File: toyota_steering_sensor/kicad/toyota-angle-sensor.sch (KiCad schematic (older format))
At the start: 32 parts, among them IC1 ATMEGA328PB-AU, IC2 LS7366R, IC3 AS5047P, J1 AVR-ISP-6, J2 RJ45, U1 NCP1117-5.0_SOT223, U2 MCP2515-xSO, U3 TJA1051T-3, Y1 16MHz, Y2 40MHz, Y3 8MHz

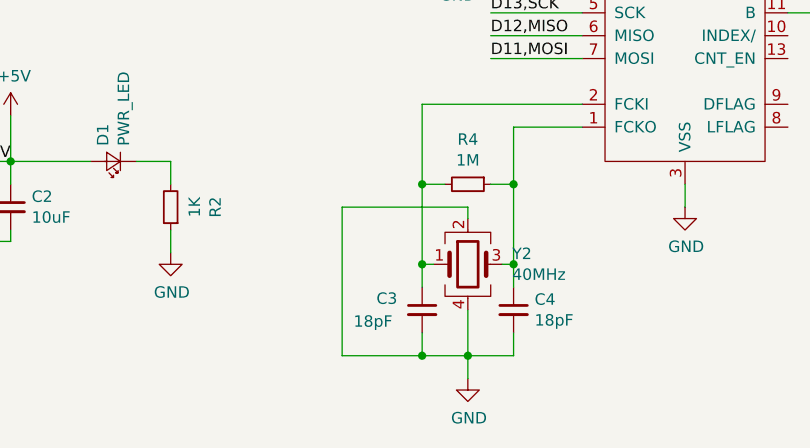
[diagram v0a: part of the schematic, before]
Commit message: change resistor and capacitor from 0402 to 0603
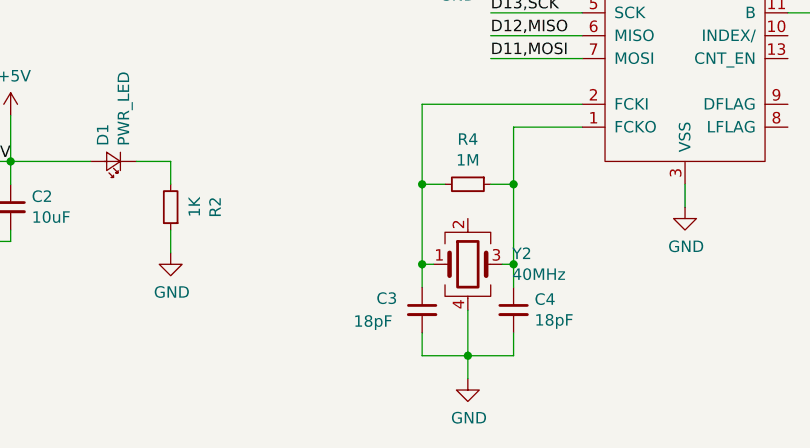
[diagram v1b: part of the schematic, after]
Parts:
- C10, C11, C12, C3, C4, C5, C6, C7, C8, C9: footprint Capacitor_SMD:C_0402_1005Metric -> Capacitor_SMD:C_0603_1608Metric
- R1, R2, R3, R4, R5, R6, R7: footprint Resistor_SMD:R_0402_1005Metric -> Resistor_SMD:R_0603_1608Metric
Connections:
- net GND: no longer Y2.2
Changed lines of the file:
@@
 F 0 "R1" H 1559 1146 50  0000 L CNN
 F 1 "10K" H 1559 1055 50  0000 L CNN
-F 2 "Resistor_SMD:R_0402_1005Metric" H 1500 1100 50  0001 C CNN
+F 2 "Resistor_SMD:R_0603_1608Metric" H 1500 1100 50  0001 C CNN
 F 3 "~" H 1500 1100 50  0001 C CNN
 	1    1500 1100
@@
 F 0 "C5" V 4321 2250 50  0000 C CNN
 F 1 "27pF" V 4412 2250 50  0000 C CNN
-F 2 "Capacitor_SMD:C_0402_1005Metric" H 4550 2250 50  0001 C CNN
+F 2 "Capacitor_SMD:C_0603_1608Metric" H 4550 2250 50  0001 C CNN
 F 3 "~" H 4550 2250 50  0001 C CNN
 	1    4550 2250
@@
 F 0 "C6" V 4413 2550 50  0000 C CNN
 F 1 "27pF" V 4412 2550 50  0001 C CNN
-F 2 "Capacitor_SMD:C_0402_1005Metric" H 4550 2550 50  0001 C CNN
+F 2 "Capacitor_SMD:C_0603_1608Metric" H 4550 2550 50  0001 C CNN
 F 3 "~" H 4550 2550 50  0001 C CNN
 	1    4550 2550
@@
 F 0 "R5" H 6459 2646 50  0000 L CNN
 F 1 "10K" H 6459 2555 50  0000 L CNN
-F 2 "Resistor_SMD:R_0402_1005Metric" H 6400 2600 50  0001 C CNN
+F 2 "Resistor_SMD:R_0603_1608Metric" H 6400 2600 50  0001 C CNN
 F 3 "~" H 6400 2600 50  0001 C CNN
 	1    6400 2600
@@
 F 0 "C7" V 8050 4100 50  0000 C CNN
 F 1 "1uF" V 7950 4100 50  0000 C CNN
-F 2 "Capacitor_SMD:C_0402_1005Metric" H 7850 4100 50  0001 C CNN
+F 2 "Capacitor_SMD:C_0603_1608Metric" H 7850 4100 50  0001 C CNN
 F 3 "~" H 7850 4100 50  0001 C CNN
 	1    7850 4100
@@
 F 0 "R3" H 3659 2696 50  0000 L CNN
 F 1 "1K" H 3659 2605 50  0000 L CNN
-F 2 "Resistor_SMD:R_0402_1005Metric" H 3600 2650 50  0001 C CNN
+F 2 "Resistor_SMD:R_0603_1608Metric" H 3600 2650 50  0001 C CNN
 F 3 "~" H 3600 2650 50  0001 C CNN
 	1    3600 2650
@@
 F 0 "C4" H 4342 5846 50  0000 L CNN
 F 1 "18pF" H 4342 5755 50  0000 L CNN
-F 2 "Capacitor_SMD:C_0402_1005Metric" H 4250 5800 50  0001 C CNN
+F 2 "Capacitor_SMD:C_0603_1608Metric" H 4250 5800 50  0001 C CNN
 F 3 "~" H 4250 5800 50  0001 C CNN
 	1    4250 5800
@@
 F 0 "R4" V 3854 5250 50  0000 C CNN
 F 1 "1M" V 3945 5250 50  0000 C CNN
-F 2 "Resistor_SMD:R_0402_1005Metric" H 4050 5250 50  0001 C CNN
+F 2 "Resistor_SMD:R_0603_1608Metric" H 4050 5250 50  0001 C CNN
 F 3 "~" H 4050 5250 50  0001 C CNN
 	1    4050 5250
@@
 F 0 "C3" H 3650 5850 50  0000 L CNN
 F 1 "18pF" H 3550 5750 50  0000 L CNN
-F 2 "Capacitor_SMD:C_0402_1005Metric" H 3850 5800 50  0001 C CNN
+F 2 "Capacitor_SMD:C_0603_1608Metric" H 3850 5800 50  0001 C CNN
 F 3 "~" H 3850 5800 50  0001 C CNN
 	1    3850 5800
@@
 F 0 "R7" H 6659 4746 50  0000 L CNN
 F 1 "10K" H 6659 4655 50  0000 L CNN
-F 2 "Resistor_SMD:R_0402_1005Metric" H 6600 4700 50  0001 C CNN
+F 2 "Resistor_SMD:R_0603_1608Metric" H 6600 4700 50  0001 C CNN
 F 3 "~" H 6600 4700 50  0001 C CNN
 	1    6600 4700
@@
 F 0 "C12" H 8392 3696 50  0000 L CNN
 F 1 ".1uF" H 8392 3605 50  0000 L CNN
-F 2 "Capacitor_SMD:C_0402_1005Metric" H 8300 3650 50  0001 C CNN
+F 2 "Capacitor_SMD:C_0603_1608Metric" H 8300 3650 50  0001 C CNN
 F 3 "~" H 8300 3650 50  0001 C CNN
 	1    8300 3650
@@
 F 0 "C9" H 4092 4196 50  0000 L CNN
 F 1 ".1uF" H 4092 4105 50  0000 L CNN
-F 2 "Capacitor_SMD:C_0402_1005Metric" H 4000 4150 50  0001 C CNN
+F 2 "Capacitor_SMD:C_0603_1608Metric" H 4000 4150 50  0001 C CNN
 F 3 "~" H 4000 4150 50  0001 C CNN
 	1    4000 4150
@@
 F 0 "C8" H 1242 3296 50  0000 L CNN
 F 1 ".1uF" H 1242 3205 50  0000 L CNN
-F 2 "Capacitor_SMD:C_0402_1005Metric" H 1150 3250 50  0001 C CNN
+F 2 "Capacitor_SMD:C_0603_1608Metric" H 1150 3250 50  0001 C CNN
 F 3 "~" H 1150 3250 50  0001 C CNN
 	1    1150 3250
@@
 F 0 "C10" H 4642 1396 50  0000 L CNN
 F 1 ".1uF" H 4642 1305 50  0000 L CNN
-F 2 "Capacitor_SMD:C_0402_1005Metric" H 4550 1350 50  0001 C CNN
+F 2 "Capacitor_SMD:C_0603_1608Metric" H 4550 1350 50  0001 C CNN
 F 3 "~" H 4550 1350 50  0001 C CNN
 	1    4550 1350
@@
 F 0 "C11" H 8192 1246 50  0000 L CNN
 F 1 ".1uF" H 8192 1155 50  0000 L CNN
-F 2 "Capacitor_SMD:C_0402_1005Metric" H 8100 1200 50  0001 C CNN
+F 2 "Capacitor_SMD:C_0603_1608Metric" H 8100 1200 50  0001 C CNN
 F 3 "~" H 8100 1200 50  0001 C CNN
 	1    8100 1200
@@
 F 0 "R2" V 2554 5350 50  0000 C CNN
 F 1 "1K" V 2645 5350 50  0000 C CNN
-F 2 "Resistor_SMD:R_0402_1005Metric" H 2750 5350 50  0001 C CNN
+F 2 "Resistor_SMD:R_0603_1608Metric" H 2750 5350 50  0001 C CNN
 F 3 "~" H 2750 5350 50  0001 C CNN
 	1    2750 5350
@@
 F 0 "R6" H 6459 3746 50  0000 L CNN
 F 1 "10K" H 6459 3655 50  0000 L CNN
-F 2 "Resistor_SMD:R_0402_1005Metric" H 6400 3700 50  0001 C CNN
+F 2 "Resistor_SMD:R_0603_1608Metric" H 6400 3700 50  0001 C CNN
 F 3 "~" H 6400 3700 50  0001 C CNN
 	1    6400 3700
 	1    0    0    -1
 $EndComp
-Wire Wire Line
-	4050 5400 4050 5350
-Wire Wire Line
-	4050 5350 3500 5350
-Wire Wire Line
-	3500 5350 3500 6000
-Wire Wire Line
-	3500 6000 3850 6000
-Connection ~ 3850 6000
 $EndSCHEMATC

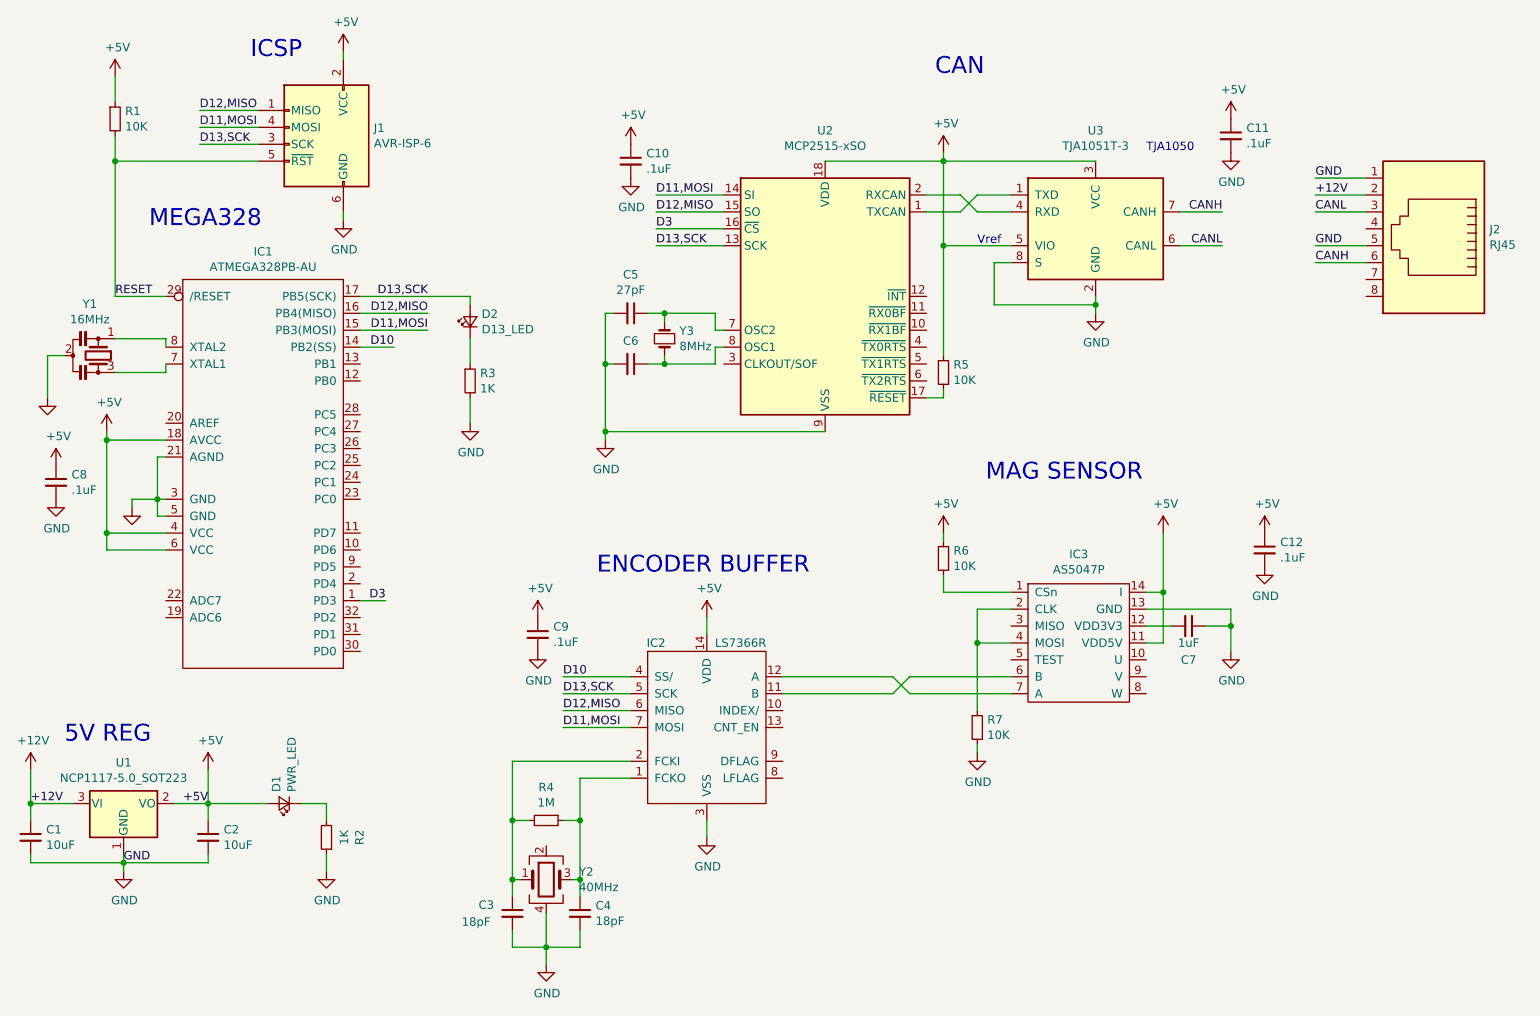
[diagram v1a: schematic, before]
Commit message: modified component ref for BOM
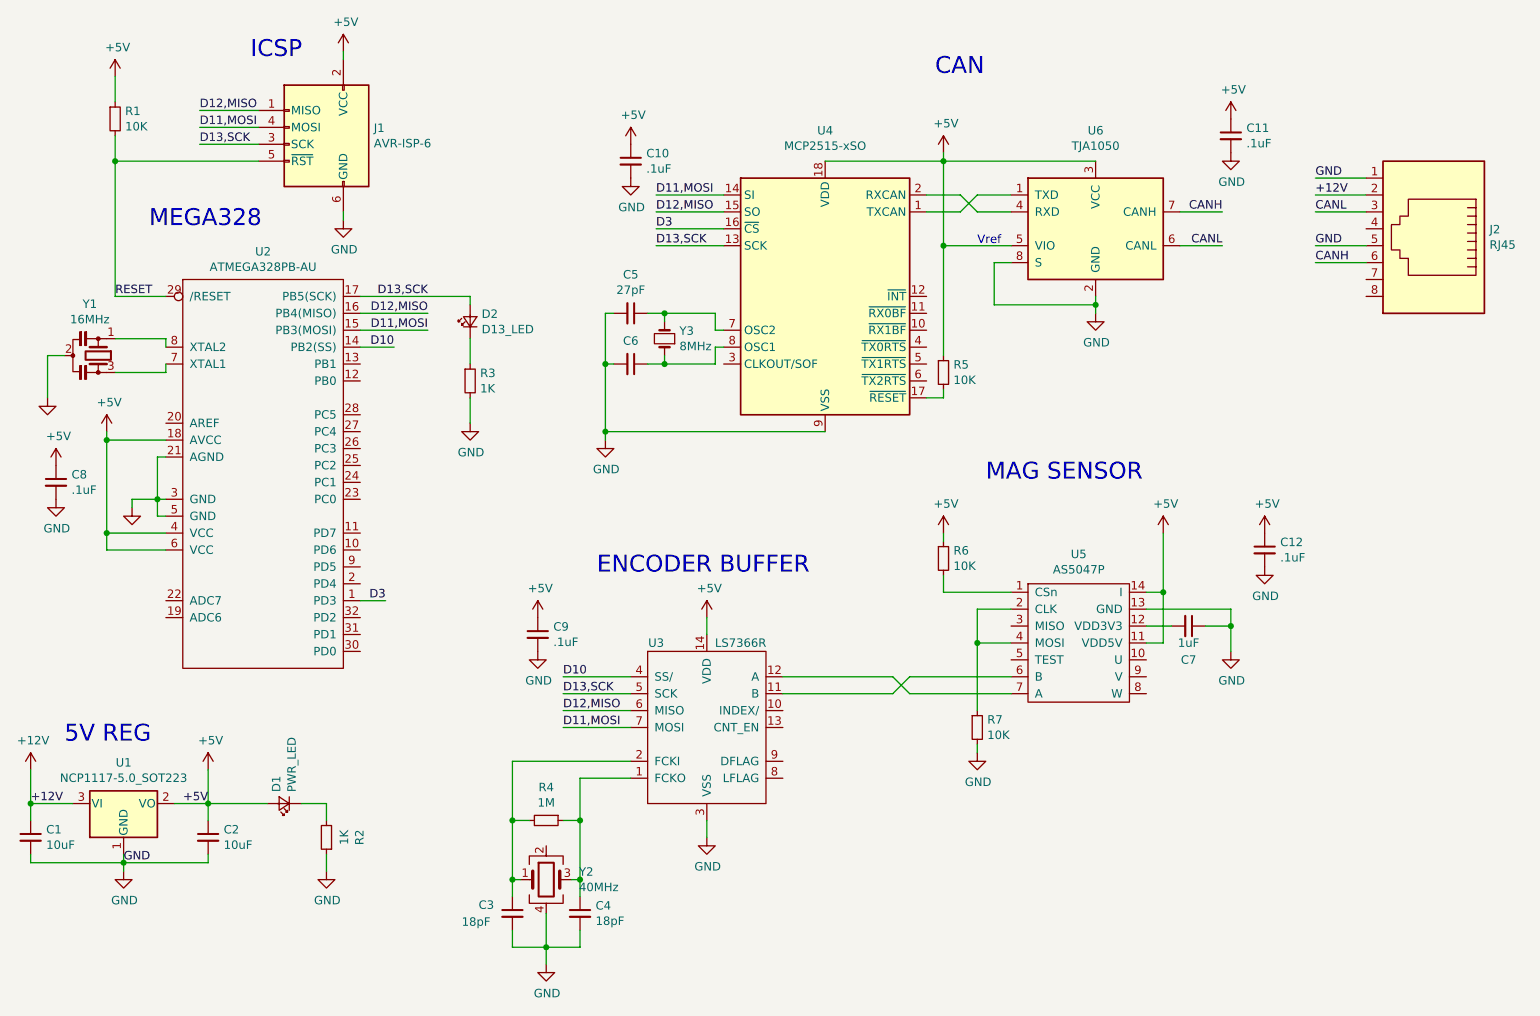
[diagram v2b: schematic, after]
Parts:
- C1, C2: Digi-Key Part Number (none) -> 490-14536-1-ND
- C10, C11, C12, C8, C9: Digi-Key Part Number (none) -> 1276-1000-1-ND
- C3, C4: Digi-Key Part Number (none) -> 1276-2208-1-ND
- C5, C6: Digi-Key Part Number (none) -> 1276-1086-1-ND
- C7: Digi-Key Part Number (none) -> 490-12297-1-ND
- D1, D2: Digi-Key Part Number (none) -> 475-1410-1-ND
- J1: Digi-Key Part Number (none) -> N/A
- J2: Digi-Key Part Number (none) -> 609-1046-ND
- R1, R5, R6, R7: Digi-Key Part Number (none) -> A130097CT-ND
- R2, R3: Digi-Key Part Number (none) -> A130091CT-ND
- R4: Digi-Key Part Number (none) -> A130109CT-ND
- U1: Digi-Key Part Number (none) -> NCP1117ST50T3GOSCT-ND
- U2: renamed from IC1; Digi-Key Part Number (none) -> ATMEGA328PB-AU-ND
- U3: renamed from IC2; Digi-Key Part Number (none) -> N/A
- U4: renamed from U2; Digi-Key Part Number (none) -> MCP2515T-I/SOCT-ND
- U5: renamed from IC3; Digi-Key Part Number (none) -> AS5047P-ATSMCT-ND
- U6: renamed from U3; value TJA1051T-3 -> TJA1050; Digi-Key Part Number (none) -> 568-10292-1-ND
- Y1: Digi-Key Part Number (none) -> 490-17948-1-ND
- Y2: Digi-Key Part Number (none) -> 535-13401-1-ND
- Y3: Digi-Key Part Number (none) -> 535-10630-1-ND
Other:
- note removed: "TJA1050"
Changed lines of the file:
@@
 F 2 "Connector_PinHeader_2.54mm:PinHeader_2x03_P2.54mm_Vertical" V 2500 1300 50  0001 C CNN
 F 3 " ~" H 1475 700 50  0001 C CNN
+F 4 "N/A" H 2750 1250 50  0001 C CNN "Digi-Key Part Number"
 	1    2750 1250
 	-1   0    0    -1
@@
 F 2 "Resistor_SMD:R_0603_1608Metric" H 1500 1100 50  0001 C CNN
 F 3 "~" H 1500 1100 50  0001 C CNN
+F 4 "A130097CT-ND" H 1500 1100 50  0001 C CNN "Digi-Key Part Number"
 	1    1500 1100
 	1    0    0    -1
@@
 F 2 "Package_TO_SOT_SMD:SOT-223-3_TabPin2" H 1550 5350 50  0001 C CNN
 F 3 "http://www.onsemi.com/pub_link/Collateral/NCP1117-D.PDF" H 1650 4900 50  0001 C CNN
+F 4 "NCP1117ST50T3GOSCT-ND" H 1550 5150 50  0001 C CNN "Digi-Key Part Number"
 	1    1550 5150
 	1    0    0    -1
@@
 F 2 "Capacitor_SMD:C_1210_3225Metric" H 1000 5350 50  0001 C CNN
 F 3 "~" H 1000 5350 50  0001 C CNN
+F 4 "490-14536-1-ND" H 1000 5350 50  0001 C CNN "Digi-Key Part Number"
 	1    1000 5350
 	1    0    0    -1
@@
 F 2 "Capacitor_SMD:C_1210_3225Metric" H 2050 5350 50  0001 C CNN
 F 3 "~" H 2050 5350 50  0001 C CNN
+F 4 "490-14536-1-ND" H 2050 5350 50  0001 C CNN "Digi-Key Part Number"
 	1    2050 5350
 	1    0    0    -1
@@
 CAN
 $Comp
-L Interface_CAN_LIN:TJA1051T-3 U3
+L Interface_CAN_LIN:TJA1051T-3 U6
 U 1 1 5D47EE70
 P 7300 1750
-F 0 "U3" H 7300 2331 50  0000 C CNN
-F 1 "TJA1051T-3" H 7300 2240 50  0000 C CNN
+F 0 "U6" H 7300 2331 50  0000 C CNN
+F 1 "TJA1050" H 7300 2240 50  0000 C CNN
 F 2 "Package_SO:SOIC-8_3.9x4.9mm_P1.27mm" H 7300 1250 50  0001 C CIN
 F 3 "http://www.nxp.com/documents/data_sheet/TJA1051.pdf" H 7300 1750 50  0001 C CNN
+F 4 "568-10292-1-ND" H 7300 1750 50  0001 C CNN "Digi-Key Part Number"
 	1    7300 1750
 	1    0    0    -1
 $EndComp
-Text Notes 7600 1300 0    50   ~ 0
-TJA1050
 Text Notes 6600 1850 0    50   ~ 0
 Vref
@@
 F 2 "Crystal:Crystal_SMD_Abracon_ABM3-2Pin_5.0x3.2mm_HandSoldering" H 4750 2400 50  0001 C CNN
 F 3 "~" H 4750 2400 50  0001 C CNN
+F 4 "535-10630-1-ND" H 4750 2400 50  0001 C CNN "Digi-Key Part Number"
 	1    4750 2400
 	0    -1   -1   0
@@
 F 2 "Capacitor_SMD:C_0603_1608Metric" H 4550 2250 50  0001 C CNN
 F 3 "~" H 4550 2250 50  0001 C CNN
+F 4 "1276-1086-1-ND " H 4550 2250 50  0001 C CNN "Digi-Key Part Number"
 	1    4550 2250
 	0    1    1    0
@@
 F 2 "Capacitor_SMD:C_0603_1608Metric" H 4550 2550 50  0001 C CNN
 F 3 "~" H 4550 2550 50  0001 C CNN
+F 4 "1276-1086-1-ND " H 4550 2550 50  0001 C CNN "Digi-Key Part Number"
 	1    4550 2550
 	0    1    1    0
@@
 F 2 "Resistor_SMD:R_0603_1608Metric" H 6400 2600 50  0001 C CNN
 F 3 "~" H 6400 2600 50  0001 C CNN
+F 4 "A130097CT-ND" H 6400 2600 50  0001 C CNN "Digi-Key Part Number"
 	1    6400 2600
 	1    0    0    -1
@@
 CANH
 $Comp
-L Angle_Sensor:AS5047P IC3
+L Angle_Sensor:AS5047P U5
 U 1 1 5D4CF604
 P 7200 3800
-F 0 "IC3" H 7200 3925 50  0000 C CNN
+F 0 "U5" H 7200 3925 50  0000 C CNN
 F 1 "AS5047P" H 7200 3834 50  0000 C CNN
 F 2 "Package_SO:TSSOP-14_4.4x5mm_P0.65mm" H 7200 3800 50  0001 C CNN
 F 3 "" H 7200 3800 50  0001 C CNN
+F 4 "AS5047P-ATSMCT-ND" H 7200 3800 50  0001 C CNN "Digi-Key Part Number"
 	1    7200 3800
 	1    0    0    -1
@@
 F 2 "Capacitor_SMD:C_0603_1608Metric" H 7850 4100 50  0001 C CNN
 F 3 "~" H 7850 4100 50  0001 C CNN
+F 4 "490-12297-1-ND" H 7850 4100 50  0001 C CNN "Digi-Key Part Number"
 	1    7850 4100
 	0    1    1    0
@@
 F 2 "LED_SMD:LED_0805_2012Metric" V 3600 2300 50  0001 C CNN
 F 3 "~" V 3600 2300 50  0001 C CNN
+F 4 "475-1410-1-ND" H 3600 2300 50  0001 C CNN "Digi-Key Part Number"
 	1    3600 2300
 	0    -1   -1   0
@@
 F 2 "Resistor_SMD:R_0603_1608Metric" H 3600 2650 50  0001 C CNN
 F 3 "~" H 3600 2650 50  0001 C CNN
+F 4 "A130091CT-ND " H 3600 2650 50  0001 C CNN "Digi-Key Part Number"
 	1    3600 2650
 	1    0    0    -1
@@
 ENCODER BUFFER
 $Comp
-L Angle_Sensor:LS7366R IC2
+L Angle_Sensor:LS7366R U3
 U 1 1 5D455878
 P 5000 4250
-F 0 "IC2" H 4700 4300 50  0000 C CNN
+F 0 "U3" H 4700 4300 50  0000 C CNN
 F 1 "LS7366R" H 5200 4300 50  0000 C CNN
 F 2 "Package_SO:SOIC-14_3.9x8.7mm_P1.27mm" H 4700 4300 50  0001 C CNN
 F 3 "" H 4700 4300 50  0001 C CNN
+F 4 "N/A" H 5000 4250 50  0001 C CNN "Digi-Key Part Number"
 	1    5000 4250
 	1    0    0    -1
@@
 	5700 2950 4400 2950
 $Comp
-L Interface_CAN_LIN:MCP2515-xSO U2
+L Interface_CAN_LIN:MCP2515-xSO U4
 U 1 1 5D479C62
 P 5700 2150
-F 0 "U2" H 5700 3131 50  0000 C CNN
+F 0 "U4" H 5700 3131 50  0000 C CNN
 F 1 "MCP2515-xSO" H 5700 3040 50  0000 C CNN
 F 2 "Package_SO:SOIC-18W_7.5x11.6mm_P1.27mm" H 5700 1250 50  0001 C CIN
 F 3 "http://ww1.microchip.com/downloads/en/DeviceDoc/21801e.pdf" H 5800 1350 50  0001 C CNN
+F 4 "MCP2515T-I/SOCT-ND" H 5700 2150 50  0001 C CNN "Digi-Key Part Number"
 	1    5700 2150
 	1    0    0    -1
@@
 F 2 "Capacitor_SMD:C_0603_1608Metric" H 4250 5800 50  0001 C CNN
 F 3 "~" H 4250 5800 50  0001 C CNN
+F 4 "1276-2208-1-ND" H 4250 5800 50  0001 C CNN "Digi-Key Part Number"
 	1    4250 5800
 	1    0    0    -1
@@
 F 2 "Resistor_SMD:R_0603_1608Metric" H 4050 5250 50  0001 C CNN
 F 3 "~" H 4050 5250 50  0001 C CNN
+F 4 "A130109CT-ND " H 4050 5250 50  0001 C CNN "Digi-Key Part Number"
 	1    4050 5250
 	0    1    1    0
@@
 F 2 "Capacitor_SMD:C_0603_1608Metric" H 3850 5800 50  0001 C CNN
 F 3 "~" H 3850 5800 50  0001 C CNN
+F 4 "1276-2208-1-ND" H 3850 5800 50  0001 C CNN "Digi-Key Part Number"
 	1    3850 5800
 	1    0    0    -1
@@
 F 2 "Resistor_SMD:R_0603_1608Metric" H 6600 4700 50  0001 C CNN
 F 3 "~" H 6600 4700 50  0001 C CNN
+F 4 "A130097CT-ND" H 6600 4700 50  0001 C CNN "Digi-Key Part Number"
 	1    6600 4700
 	1    0    0    -1
@@
 F 2 "Connector_RJ:RJ45_Amphenol_54602-x08_Horizontal" V 9300 1775 50  0001 C CNN
 F 3 "~" V 9300 1775 50  0001 C CNN
+F 4 "609-1046-ND" H 9300 1750 50  0001 C CNN "Digi-Key Part Number"
 	1    9300 1750
 	-1   0    0    1
@@
 F 2 "Crystal:Resonator_SMD_muRata_CSTxExxV-3Pin_3.0x1.1mm_HandSoldering" H 1375 2500 50  0001 C CNN
 F 3 "~" H 1375 2500 50  0001 C CNN
+F 4 "490-17948-1-ND" H 1400 2500 50  0001 C CNN "Digi-Key Part Number"
 	1    1400 2500
 	0    1    1    0
 $EndComp
 $Comp
-L Angle_Sensor:ATMEGA328PB-AU IC1
+L Angle_Sensor:ATMEGA328PB-AU U2
 U 1 1 5D43444B
 P 2400 1950
-F 0 "IC1" H 2375 2015 50  0000 C CNN
+F 0 "U2" H 2375 2015 50  0000 C CNN
 F 1 "ATMEGA328PB-AU" H 2375 1924 50  0000 C CNN
 F 2 "Package_QFP:TQFP-32_7x7mm_P0.8mm" H 2400 -500 50  0001 C CNN
 F 3 "" H 2400 -500 50  0001 C CNN
+F 4 "ATMEGA328PB-AU-ND" H 2400 1950 50  0001 C CNN "Digi-Key Part Number"
 	1    2400 1950
 	1    0    0    -1
@@
 F 2 "Capacitor_SMD:C_0603_1608Metric" H 8300 3650 50  0001 C CNN
 F 3 "~" H 8300 3650 50  0001 C CNN
+F 4 "1276-1000-1-ND" H 8300 3650 50  0001 C CNN "Digi-Key Part Number"
 	1    8300 3650
 	1    0    0    -1
@@
 F 2 "Capacitor_SMD:C_0603_1608Metric" H 4000 4150 50  0001 C CNN
 F 3 "~" H 4000 4150 50  0001 C CNN
+F 4 "1276-1000-1-ND" H 4000 4150 50  0001 C CNN "Digi-Key Part Number"
 	1    4000 4150
 	1    0    0    -1
@@
 F 2 "Capacitor_SMD:C_0603_1608Metric" H 1150 3250 50  0001 C CNN
 F 3 "~" H 1150 3250 50  0001 C CNN
+F 4 "1276-1000-1-ND" H 1150 3250 50  0001 C CNN "Digi-Key Part Number"
 	1    1150 3250
 	1    0    0    -1
@@
 F 2 "Capacitor_SMD:C_0603_1608Metric" H 4550 1350 50  0001 C CNN
 F 3 "~" H 4550 1350 50  0001 C CNN
+F 4 "1276-1000-1-ND" H 4550 1350 50  0001 C CNN "Digi-Key Part Number"
 	1    4550 1350
 	1    0    0    -1
@@
 F 2 "Capacitor_SMD:C_0603_1608Metric" H 8100 1200 50  0001 C CNN
 F 3 "~" H 8100 1200 50  0001 C CNN
+F 4 "1276-1000-1-ND" H 8100 1200 50  0001 C CNN "Digi-Key Part Number"
 	1    8100 1200
 	1    0    0    -1
@@
 F 2 "Crystal:Crystal_SMD_Abracon_ABM8G-4Pin_3.2x2.5mm" H 4050 5600 50  0001 C CNN
 F 3 "~" H 4050 5600 50  0001 C CNN
+F 4 "535-13401-1-ND" H 4050 5600 50  0001 C CNN "Digi-Key Part Number"
 	1    4050 5600
 	1    0    0    -1
@@
 F 2 "Resistor_SMD:R_0603_1608Metric" H 2750 5350 50  0001 C CNN
 F 3 "~" H 2750 5350 50  0001 C CNN
+F 4 "A130091CT-ND " H 2750 5350 50  0001 C CNN "Digi-Key Part Number"
 	1    2750 5350
 	-1   0    0    1
@@
 F 2 "LED_SMD:LED_0805_2012Metric" V 2500 5150 50  0001 C CNN
 F 3 "~" V 2500 5150 50  0001 C CNN
+F 4 "475-1410-1-ND" H 2500 5150 50  0001 C CNN "Digi-Key Part Number"
 	1    2500 5150
 	-1   0    0    1
@@
 F 2 "Resistor_SMD:R_0603_1608Metric" H 6400 3700 50  0001 C CNN
 F 3 "~" H 6400 3700 50  0001 C CNN
+F 4 "A130097CT-ND" H 6400 3700 50  0001 C CNN "Digi-Key Part Number"
 	1    6400 3700
 	1    0    0    -1
